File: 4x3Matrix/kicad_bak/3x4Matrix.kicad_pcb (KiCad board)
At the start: 2 copper layers, 99.4 x 49.5 mm, 56 parts, among them M1 AudioJack, M2 AudioJack, M3 AudioJack, M4 AudioJack, U1 TL074_SMD, U2 TL072_SMD

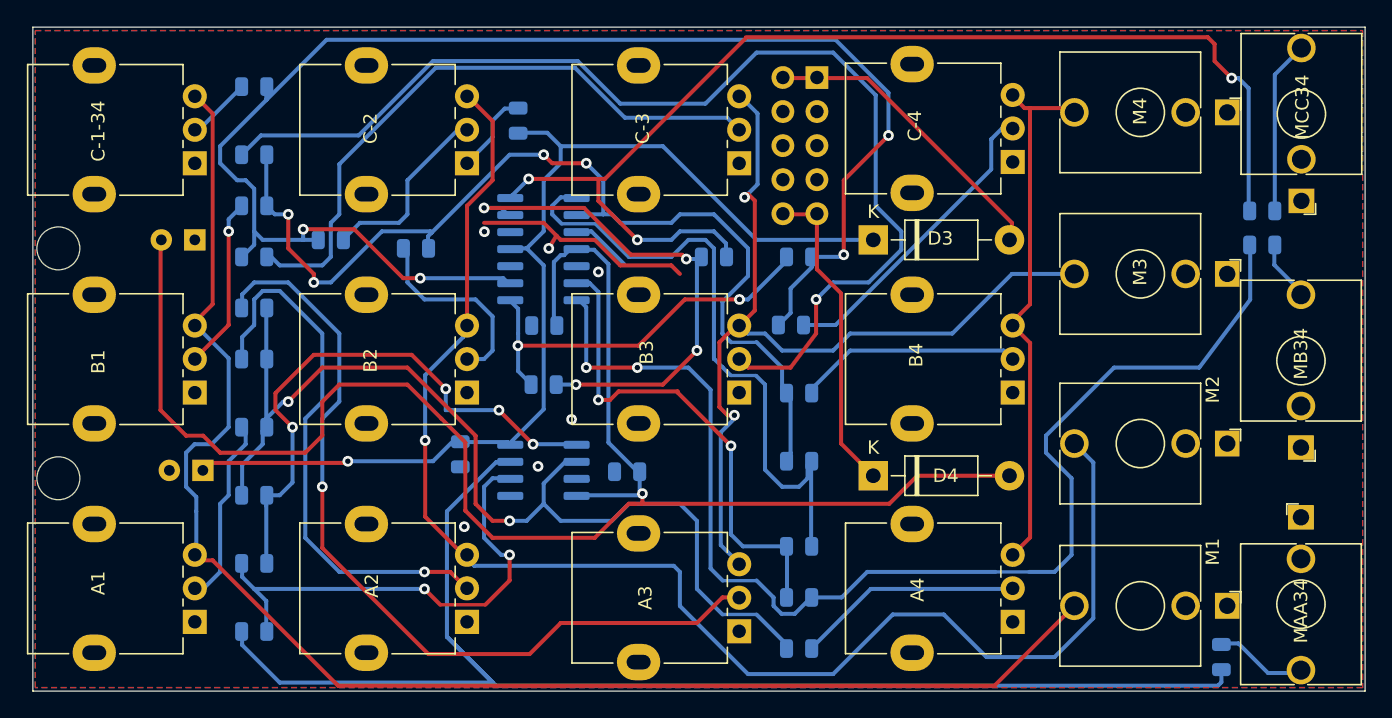
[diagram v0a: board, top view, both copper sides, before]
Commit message: All library parts replaced by default Kicad, new version created which uses 3 TL072 instead of TL072 + TL074 to eliminate crosstalk
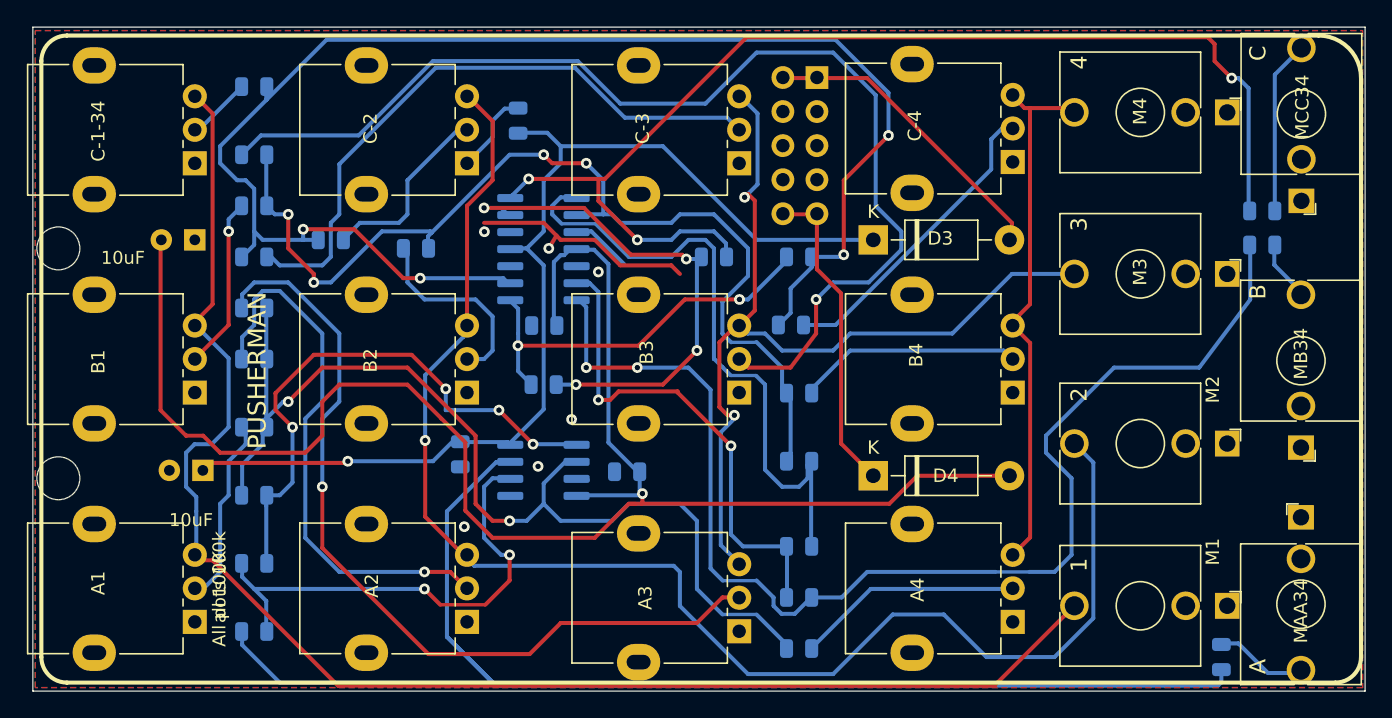
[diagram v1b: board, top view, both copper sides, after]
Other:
- board text added: "1"
- board text added: "100n"
- board text added: "10uF"
- board text added: "2"
- board text added: "3"
- board text added: "3x4 Matrix"
- board text added: "4"
- board text added: "A"
- board text added: "A gain"
- board text added: "All pots 100k"
- board text added: "B"
- board text added: "B gain"
- board text added: "C"
- board text added: "C gain"
- board text added: "C9"
- board text added: "PUSHERMAN"
- board text added: "TL072"
- board text added: "TL074"
- board text added: "all 100K"
- board text added: "all 100k"
